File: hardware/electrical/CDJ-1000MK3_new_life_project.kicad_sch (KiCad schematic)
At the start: 0 parts

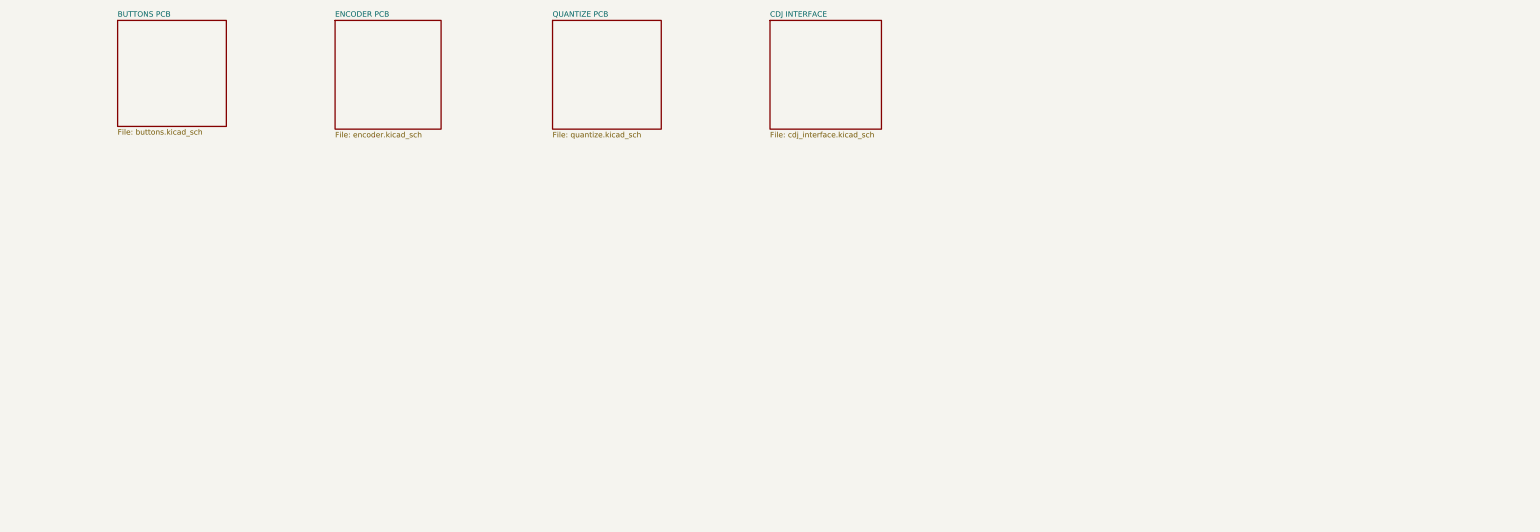
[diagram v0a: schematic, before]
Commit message: Schematic rev. 2 Add second microcontroller to handle encoder, buttons and LEDs Remove external pull-up resistors Simplify LED driver circuits Remove debouncing capacitors Rename SPI connections with standard names Use SPI1 rather than SPI2 Isolate GNDD and GLED
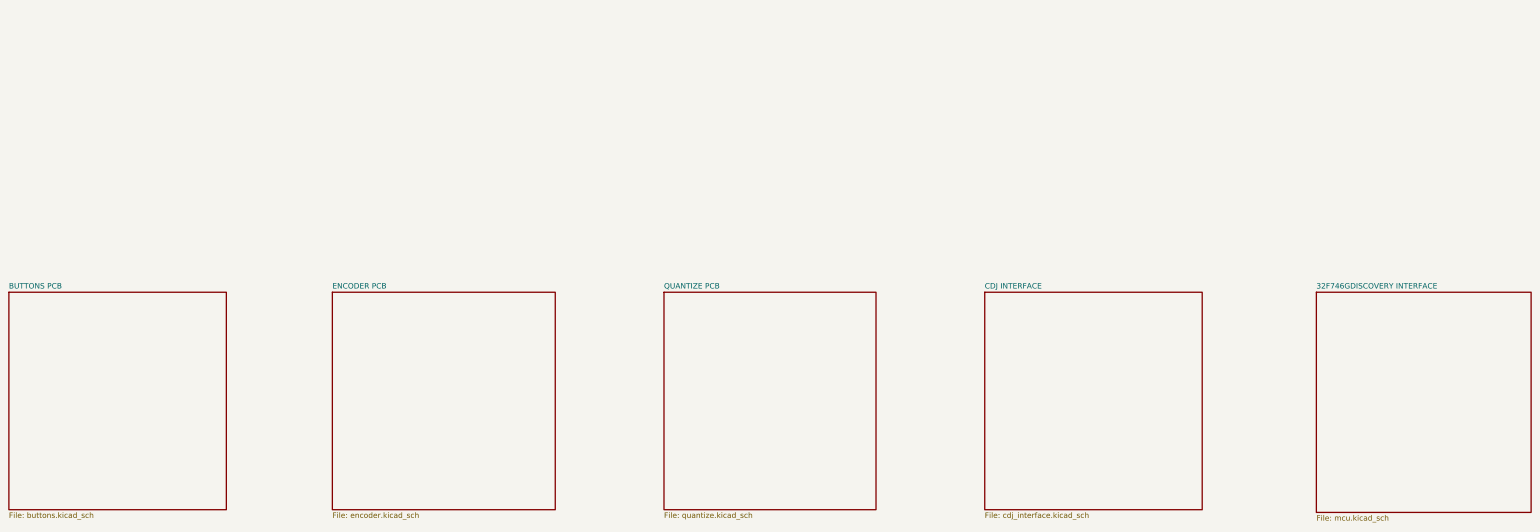
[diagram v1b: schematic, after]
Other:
- added sheet 32F746GDISCOVERY INTERFACE (mcu.kicad_sch)
- company: © ANDREI ANATSKO, FRANK PLOWMAN 2022 -> © ANDREI ANATSKA, FRANK PLOWMAN 2022
